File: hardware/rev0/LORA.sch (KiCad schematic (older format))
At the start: 29 parts, among them U1 WT325BI0032.000000, U2 SX1276

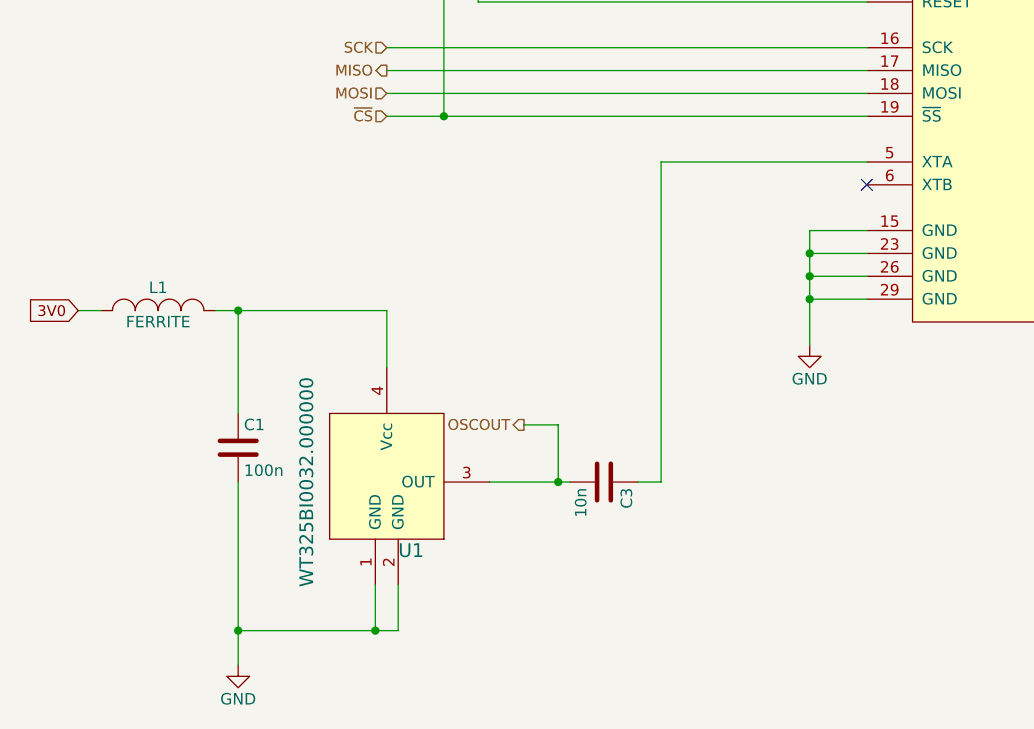
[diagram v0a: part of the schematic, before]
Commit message: Replace TCXO with XTAL
Planned TCXO became obsolete and hard to source, high quality XTAL
should be good enough with possible temperature compensation in
software.
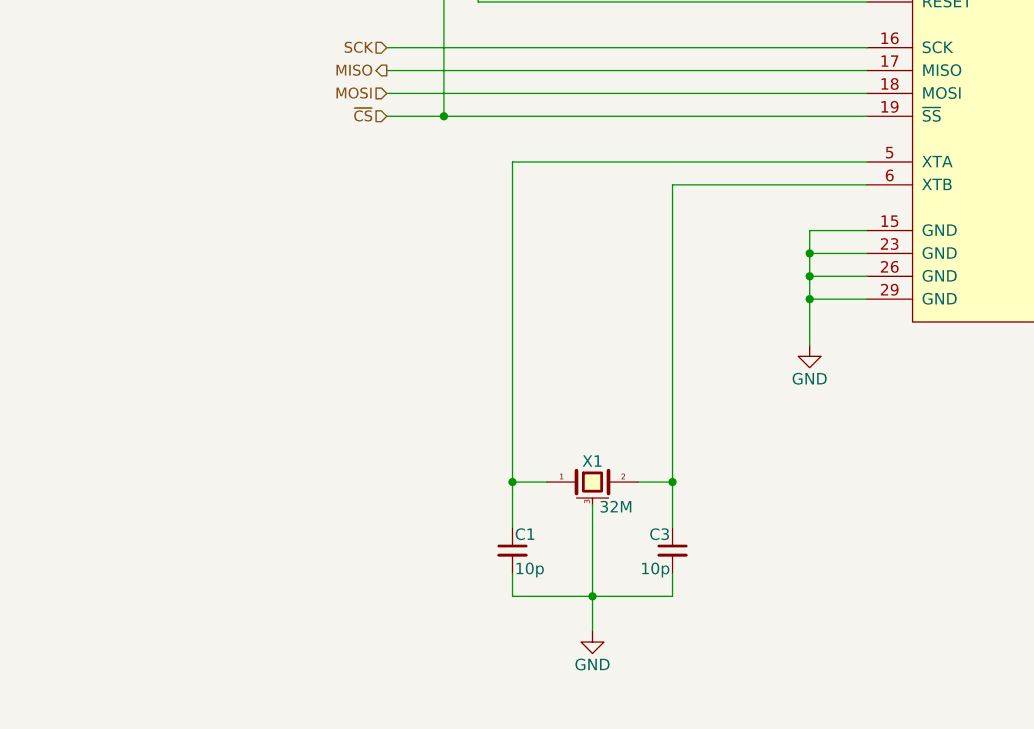
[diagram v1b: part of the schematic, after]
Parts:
- removed C1: 100n, Capacitors_SMD:C_0402, symbol C
- removed C3: 10n, Capacitors_SMD:C_0402, symbol C
- removed L1: FERRITE, Resistors_SMD:R_0603, symbol INDUCTOR_SMALL
- removed U1: WT325BI0032.000000, Custom Parts:TCXO-WT325, symbol WT325-TCXO
- added C1, C3: 10p, Capacitors_SMD:C_0402, symbol C_Small
- added X1: 32M, Custom Parts:XTAL-2x2.5, symbol CRYSTAL_SMD
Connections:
- net GND: now also C1.2, C3.2, X1.3 (case)
- net at U2.5 (XTA): now also C1.1, X1.1
- net at U2.6 (XTB): now also C3.1, X1.2
- no-connect marks 9 -> 8
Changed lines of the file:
@@
-	1    0    0    -1
-$EndComp
-$Comp
-L WT325-TCXO U1
-U 1 1 5637AEFA
-P 2100 5250
-F 0 "U1" H 2150 4950 60  0000 L CNN
-F 1 "WT325BI0032.000000" V 1750 5250 60  0000 C CNN
-F 2 "Custom Parts:TCXO-WT325" H 2100 5250 60  0001 C CNN
-F 3 "" H 2100 5250 60  0000 C CNN
-	1    2100 5250
 	1    0    0    -1
 $EndComp
@@
 Text HLabel 2100 3450 0    47   Output ~ 0
 MISO
-$Comp
-L INDUCTOR_SMALL L1
-U 1 1 5637B5A3
-P 1100 4500
-F 0 "L1" H 1100 4600 50  0000 C CNN
-F 1 "FERRITE" H 1100 4450 50  0000 C CNN
-F 2 "Resistors_SMD:R_0603" H 1100 4500 60  0001 C CNN
-F 3 "" H 1100 4500 60  0000 C CNN
-	1    1100 4500
-	1    0    0    -1
-$EndComp
-Text GLabel 750  4500 0    47   Input ~ 0
-3V0
-$Comp
-L C C1
-U 1 1 5637BB20
-P 1450 5100
-F 0 "C1" H 1475 5200 50  0000 L CNN
-F 1 "100n" H 1475 5000 50  0000 L CNN
-F 2 "Capacitors_SMD:C_0402" H 1488 4950 30  0001 C CNN
-F 3 "" H 1450 5100 60  0000 C CNN
-	1    1450 5100
-	1    0    0    -1
-$EndComp
-$Comp
-L GND #PWR05
-U 1 1 5637BCDF
-P 1450 6050
-F 0 "#PWR05" H 1450 5800 50  0001 C CNN
-F 1 "GND" H 1450 5900 50  0000 C CNN
-F 2 "" H 1450 6050 60  0000 C CNN
-F 3 "" H 1450 6050 60  0000 C CNN
-	1    1450 6050
-	1    0    0    -1
-$EndComp
-$Comp
-L C C3
-U 1 1 5637BD6D
-P 3050 5250
-F 0 "C3" H 3075 5350 50  0000 L CNN
-F 1 "10n" H 3075 5150 50  0000 L CNN
-F 2 "Capacitors_SMD:C_0402" H 3088 5100 30  0001 C CNN
-F 3 "" H 3050 5250 60  0000 C CNN
-	1    3050 5250
-	0    1    1    0
-$EndComp
-NoConn ~ 4200 3950
 NoConn ~ 7000 2350
 NoConn ~ 7000 3450
@@
 $EndComp
 $Comp
-L GND #PWR06
+L GND #PWR05
 U 1 1 5637E039
 P 7450 3450
-F 0 "#PWR06" H 7450 3200 50  0001 C CNN
+F 0 "#PWR05" H 7450 3200 50  0001 C CNN
 F 1 "GND" H 7450 3300 50  0000 C CNN
 F 2 "" H 7450 3450 60  0000 C CNN
@@
 ANT
 $Comp
-L GND #PWR07
+L GND #PWR06
 U 1 1 56380EFC
 P 7450 950
-F 0 "#PWR07" H 7450 700 50  0001 C CNN
+F 0 "#PWR06" H 7450 700 50  0001 C CNN
 F 1 "GND" H 7450 800 50  0000 C CNN
 F 2 "" H 7450 950 60  0000 C CNN
@@
 Connection ~ 2500 1650
 Wire Wire Line
-	1350 4500 2100 4500
-Wire Wire Line
-	2100 4500 2100 4750
-Wire Wire Line
-	750  4500 850  4500
-Wire Wire Line
-	1450 4950 1450 4500
-Connection ~ 1450 4500
-Wire Wire Line
-	1450 5250 1450 6050
-Wire Wire Line
-	1450 5900 2150 5900
-Wire Wire Line
-	2150 5900 2150 5700
-Wire Wire Line
-	2050 5700 2050 5900
-Connection ~ 2050 5900
-Connection ~ 1450 5900
-Wire Wire Line
-	4200 3850 3300 3850
-Wire Wire Line
-	3300 3850 3300 5250
-Wire Wire Line
-	3300 5250 3200 5250
-Wire Wire Line
-	2550 5250 2900 5250
+	2650 3850 4200 3850
 Wire Wire Line
 	7050 3350 7000 3350
@@
 Wire Wire Line
 	2500 3150 4200 3150
-Text HLabel 2700 5000 0    47   Output ~ 0
-OSCOUT
-Wire Wire Line
-	2700 5000 2850 5000
-Wire Wire Line
-	2850 5000 2850 5250
-Connection ~ 2850 5250
+$Comp
+L CRYSTAL_SMD X1
+U 1 1 56A7EA30
+P 3000 5250
+F 0 "X1" H 3000 5340 50  0000 C CNN
+F 1 "32M" H 3030 5140 50  0000 L CNN
+F 2 "Custom Parts:XTAL-2x2.5" H 3000 5250 50  0001 C CNN
+F 3 "" H 3000 5250 50  0000 C CNN
+	1    3000 5250
+	1    0    0    -1
+$EndComp
+Wire Wire Line
+	3350 5250 3200 5250
+Wire Wire Line
+	2650 5250 2800 5250
+Wire Wire Line
+	2650 3850 2650 5450
+Wire Wire Line
+	3350 3950 3350 5450
+Wire Wire Line
+	3350 3950 4200 3950
+$Comp
+L C_Small C1
+U 1 1 56A7F222
+P 2650 5550
+F 0 "C1" H 2660 5620 50  0000 L CNN
+F 1 "10p" H 2660 5470 50  0000 L CNN
+F 2 "Capacitors_SMD:C_0402" H 2650 5550 50  0001 C CNN
+F 3 "" H 2650 5550 50  0000 C CNN
+	1    2650 5550
+	1    0    0    -1
+$EndComp
+$Comp
+L C_Small C3
+U 1 1 56A7F307
+P 3350 5550
+F 0 "C3" H 3360 5620 50  0000 L CNN
+F 1 "10p" H 3360 5470 50  0000 L CNN
+F 2 "Capacitors_SMD:C_0402" H 3350 5550 50  0001 C CNN
+F 3 "" H 3350 5550 50  0000 C CNN
+	1    3350 5550
+	-1   0    0    -1
+$EndComp
+Connection ~ 3350 5250
+Connection ~ 2650 5250
+Wire Wire Line
+	3000 5350 3000 5900
+Wire Wire Line
+	2650 5750 3350 5750
+Wire Wire Line
+	2650 5750 2650 5650
+Wire Wire Line
+	3350 5750 3350 5650
+Connection ~ 3000 5750
+$Comp
+L GND #PWR07
+U 1 1 56A7F767
+P 3000 5900
+F 0 "#PWR07" H 3000 5650 50  0001 C CNN
+F 1 "GND" H 3000 5750 50  0000 C CNN
+F 2 "" H 3000 5900 50  0000 C CNN
+F 3 "" H 3000 5900 50  0000 C CNN
+	1    3000 5900
+	1    0    0    -1
+$EndComp
 $EndSCHEMATC
